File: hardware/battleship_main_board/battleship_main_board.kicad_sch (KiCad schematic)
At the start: 5 parts

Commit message: Work on main board
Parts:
- removed R?: R, symbol Device:R
- removed U? (x4): 74HC595, symbol 74xx:74HC595
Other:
- removed sheet InputMatrix
- added sheet ESP32 (esp32.kicad_sch)
- added sheet OutputMatrix (outtputmatrix.kicad_sch)
- added sheet OutputMatrix1 (outtputmatrix.kicad_sch)
- added sheet UserInputs (user_inputs.kicad_sch)

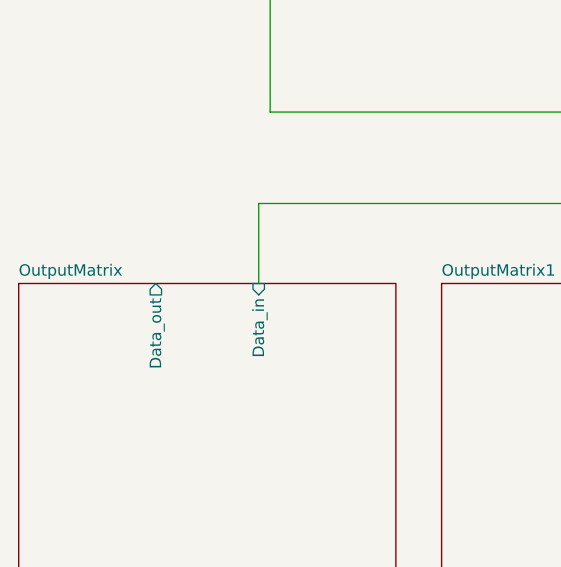
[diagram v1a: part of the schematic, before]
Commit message: Got schematic to place that can be turned into a ratsnest
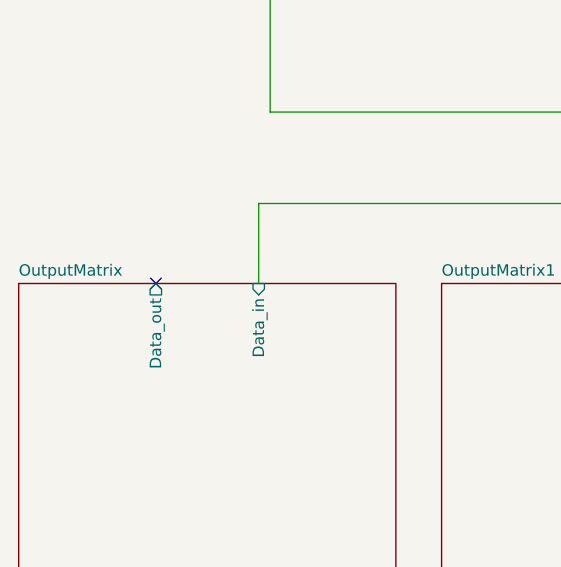
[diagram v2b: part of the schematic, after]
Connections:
- no-connect marks 0 -> 1

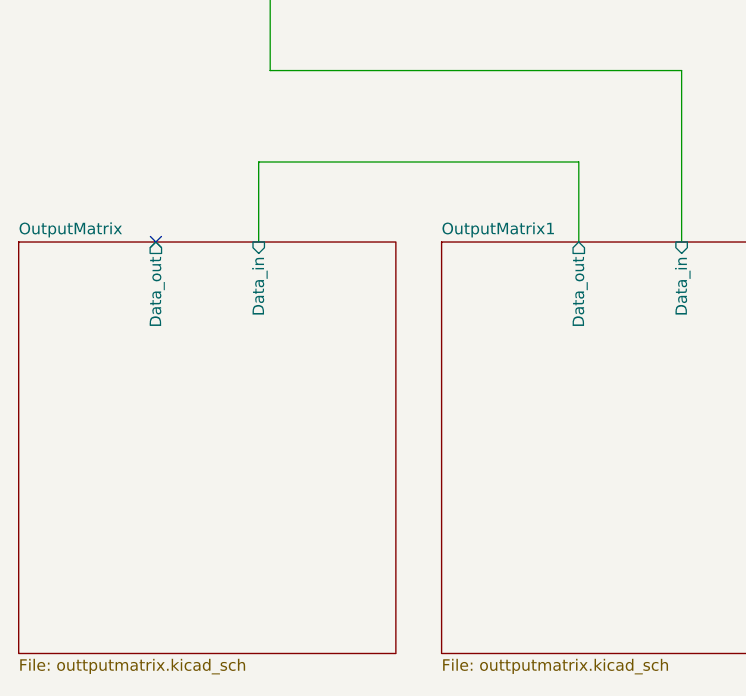
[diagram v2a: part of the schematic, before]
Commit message: Fixed annotations so that button rows are in order
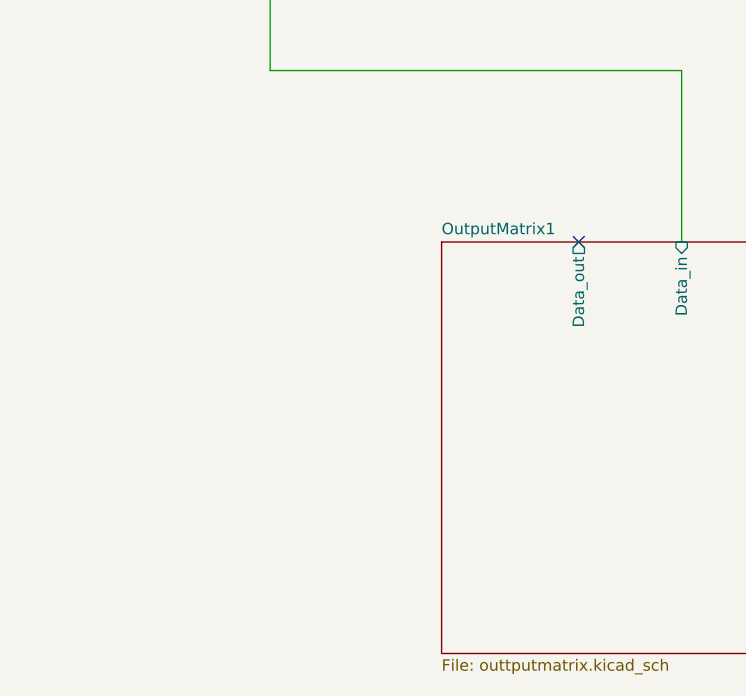
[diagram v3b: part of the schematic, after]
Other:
- removed sheet OutputMatrix
